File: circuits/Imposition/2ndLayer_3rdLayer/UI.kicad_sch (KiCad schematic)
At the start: 21 parts, among them Q15 2N7002, SW5 SW_DIP_x04, SW6 SW_SPDT

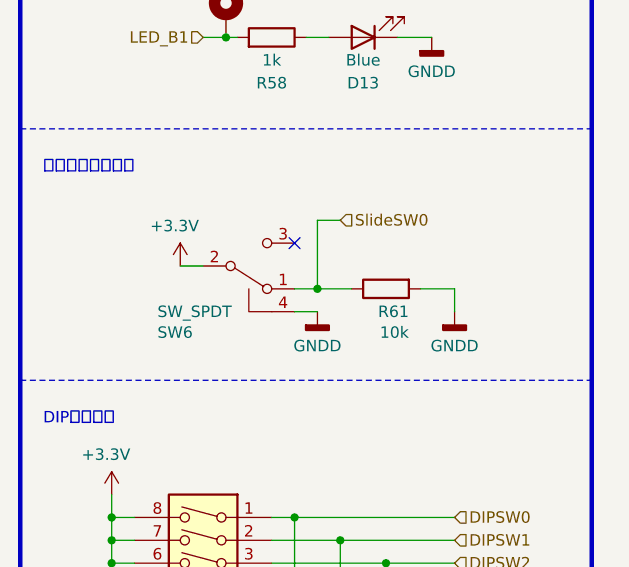
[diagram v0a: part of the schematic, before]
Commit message: 発注_第一弾
Drive, 1stLayer_Power, 2ndLayer_3rdLayer
を発注
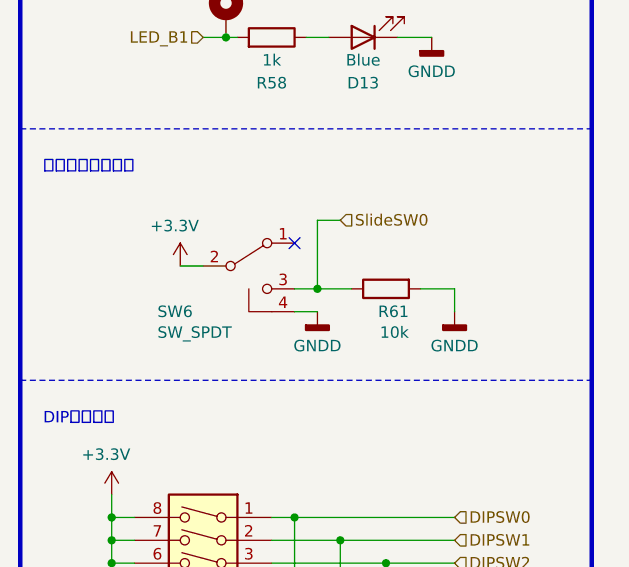
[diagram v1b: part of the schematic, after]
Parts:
- R66: footprint Resistor_SMD:R_0402_1005Metric -> Resistor_SMD:R_0603_1608Metric
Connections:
- net SlideSW0: now also SW6.3 (C); no longer SW6.1 (A)
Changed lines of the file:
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@@
       (effects (font (size 1.27 1.27)))
     )
-    (property "Footprint" "Resistor_SMD:R_0402_1005Metric" (at 175.26 131.318 90)
+    (property "Footprint" "Resistor_SMD:R_0603_1608Metric" (at 175.26 131.318 90)
       (effects (font (size 1.27 1.27)) hide)
     )
@@
     )
   )
-  (symbol (lib_id "Switch:SW_SPDT") (at 99.06 101.6 0) (mirror x) (unit 1)
+  (symbol (lib_id "Switch:SW_SPDT") (at 99.06 101.6 0) (unit 1)
     (in_bom yes) (on_board yes) (dnp no)
-    (property "Reference" "SW6" (at 88.9 108.9914 0)
+    (property "Reference" "SW6" (at 88.9 106.68 0)
       (effects (font (size 1.27 1.27)) (justify left))
     )
-    (property "Value" "SW_SPDT" (at 88.9 106.68 0)
+    (property "Value" "SW_SPDT" (at 88.9 108.9914 0)
       (effects (font (size 1.27 1.27)) (justify left))
     )
